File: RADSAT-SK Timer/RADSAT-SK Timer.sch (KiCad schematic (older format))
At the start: 72 parts, among them J101 Conn_02x26_Odd_Even, J103 Conn_02x26_Odd_Even, Q101 IRLML2060, Q102 IRLML2060, Q103 IRLML2060, Q104 IRLML2060, Q105 IRLML2060, Q106 IRLML2060, Q107 IRLML2060, Q108 IRLML2060, Q109 IRLML2060, U101 LM397MF, U102 LM397MF, U103 LM397MF, U104 CD4052B

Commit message: Sourced coin cell battery and tantalum caps, still need to footprint coin cell holders
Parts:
- C101, C102, C105, C106, C107, C108: footprint Capacitor_Tantalum_SMD:CP_EIA-7343-31_Kemet-D -> Capacitor_Tantalum_SMD:CP_EIA-7343-30_AVX-N_Pad2.25x2.55mm_HandSolder
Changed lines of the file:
@@
 F 0 "C101" H 2593 1721 50  0000 L CNN
 F 1 "330u" H 2593 1630 50  0000 L CNN
-F 2 "Capacitor_Tantalum_SMD:CP_EIA-7343-31_Kemet-D" H 2513 1525 50  0001 C CNN
+F 2 "Capacitor_Tantalum_SMD:CP_EIA-7343-30_AVX-N_Pad2.25x2.55mm_HandSolder" H 2513 1525 50  0001 C CNN
 F 3 "~" H 2475 1675 50  0001 C CNN
 	1    2475 1675
@@
 F 0 "C102" H 2993 1721 50  0000 L CNN
 F 1 "330u" H 2993 1630 50  0000 L CNN
-F 2 "Capacitor_Tantalum_SMD:CP_EIA-7343-31_Kemet-D" H 2913 1525 50  0001 C CNN
+F 2 "Capacitor_Tantalum_SMD:CP_EIA-7343-30_AVX-N_Pad2.25x2.55mm_HandSolder" H 2913 1525 50  0001 C CNN
 F 3 "~" H 2875 1675 50  0001 C CNN
 	1    2875 1675
@@
 F 0 "C105" H 2593 3821 50  0000 L CNN
 F 1 "330u" H 2593 3730 50  0000 L CNN
-F 2 "Capacitor_Tantalum_SMD:CP_EIA-7343-31_Kemet-D" H 2513 3625 50  0001 C CNN
+F 2 "Capacitor_Tantalum_SMD:CP_EIA-7343-30_AVX-N_Pad2.25x2.55mm_HandSolder" H 2513 3625 50  0001 C CNN
 F 3 "~" H 2475 3775 50  0001 C CNN
 	1    2475 3775
@@
 F 0 "C107" H 2993 3821 50  0000 L CNN
 F 1 "330u" H 2993 3730 50  0000 L CNN
-F 2 "Capacitor_Tantalum_SMD:CP_EIA-7343-31_Kemet-D" H 2913 3625 50  0001 C CNN
+F 2 "Capacitor_Tantalum_SMD:CP_EIA-7343-30_AVX-N_Pad2.25x2.55mm_HandSolder" H 2913 3625 50  0001 C CNN
 F 3 "~" H 2875 3775 50  0001 C CNN
 	1    2875 3775
@@
 F 0 "C106" H 2593 5871 50  0000 L CNN
 F 1 "330u" H 2593 5780 50  0000 L CNN
-F 2 "Capacitor_Tantalum_SMD:CP_EIA-7343-31_Kemet-D" H 2513 5675 50  0001 C CNN
+F 2 "Capacitor_Tantalum_SMD:CP_EIA-7343-30_AVX-N_Pad2.25x2.55mm_HandSolder" H 2513 5675 50  0001 C CNN
 F 3 "~" H 2475 5825 50  0001 C CNN
 	1    2475 5825
@@
 F 0 "C108" H 2993 5871 50  0000 L CNN
 F 1 "330u" H 2993 5780 50  0000 L CNN
-F 2 "Capacitor_Tantalum_SMD:CP_EIA-7343-31_Kemet-D" H 2913 5675 50  0001 C CNN
+F 2 "Capacitor_Tantalum_SMD:CP_EIA-7343-30_AVX-N_Pad2.25x2.55mm_HandSolder" H 2913 5675 50  0001 C CNN
 F 3 "~" H 2875 5825 50  0001 C CNN
 	1    2875 5825

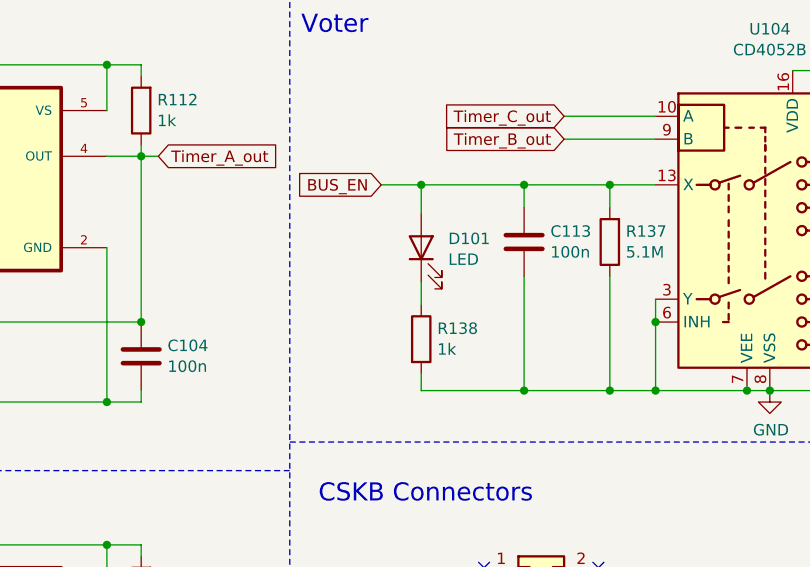
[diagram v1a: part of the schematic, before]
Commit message: the RBF relay transistor was redundant, added in another LED and updated diode configuration, resistor sourcing TBD
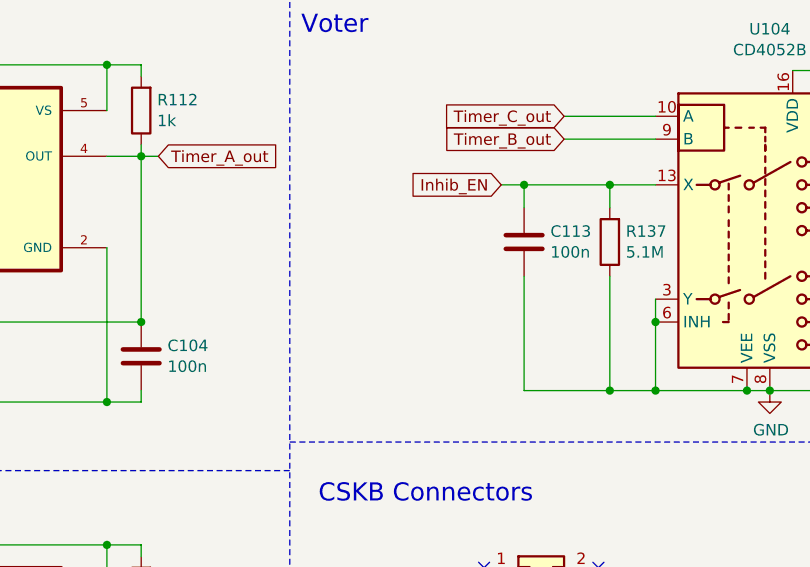
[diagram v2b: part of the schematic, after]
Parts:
- removed D101: LED, LED_SMD:LED_0603_1608Metric_Pad1.05x0.95mm_HandSolder, symbol Device:LED
- removed R138: 1k, Resistor_SMD:R_0805_2012Metric, symbol Device:R
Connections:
- net BUS_EN renamed Inhib_EN
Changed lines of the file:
@@
 Wire Wire Line
 	8225 1075 8625 1075
-Text GLabel 7425 1275 0    50   Input ~ 0
-BUS_EN
+Text GLabel 7950 1275 0    50   Input ~ 0
+Inhib_EN
 Wire Wire Line
 	9750 1325 9750 1275
@@
 	8050 2175 8425 2175
 Connection ~ 8425 2175
-Connection ~ 8050 1275
 Wire Wire Line
 	10775 775  10775 1400
@@
 NoConn ~ 10350 4225
 NoConn ~ 10350 4125
-$Comp
-L Device:LED D101
-U 1 1 600FEA55
-P 7600 1550
-F 0 "D101" V 7639 1432 50  0000 R CNN
-F 1 "LED" V 7548 1432 50  0000 R CNN
-F 2 "LED_SMD:LED_0603_1608Metric_Pad1.05x0.95mm_HandSolder" H 7600 1550 50  0001 C CNN
-F 3 "~" H 7600 1550 50  0001 C CNN
-	1    7600 1550
-	0    -1   -1   0
-$EndComp
-$Comp
-L Device:R R138
-U 1 1 60100324
-P 7600 1950
-F 0 "R138" H 7670 1996 50  0000 L CNN
-F 1 "1k" H 7670 1905 50  0000 L CNN
-F 2 "Resistor_SMD:R_0805_2012Metric" V 7530 1950 50  0001 C CNN
-F 3 "~" H 7600 1950 50  0001 C CNN
-	1    7600 1950
-	1    0    0    -1
-$EndComp
-Wire Wire Line
-	7600 1700 7600 1800
-Wire Wire Line
-	7600 1400 7600 1275
-Wire Wire Line
-	7600 1275 8050 1275
-Wire Wire Line
-	7600 1275 7425 1275
-Connection ~ 7600 1275
-Wire Wire Line
-	7600 2100 7600 2175
-Wire Wire Line
-	7600 2175 8050 2175
-Connection ~ 8050 2175
 Wire Wire Line
 	2100 2850 2875 2850
@@
 Wire Wire Line
 	8375 4150 8800 4150
+Connection ~ 8050 1275
+Wire Wire Line
+	7950 1275 8050 1275
 $EndSCHEMATC

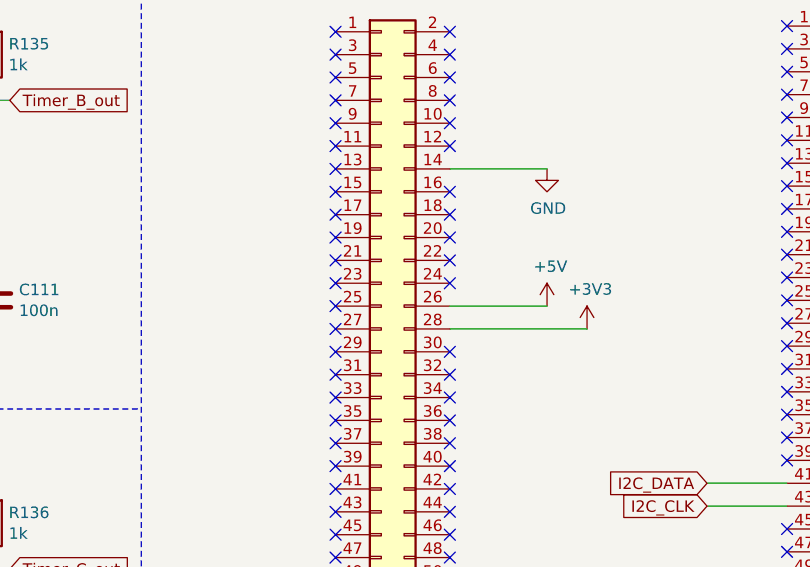
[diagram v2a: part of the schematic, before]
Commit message: Made changes to accomadate the RBF alternate charge plug
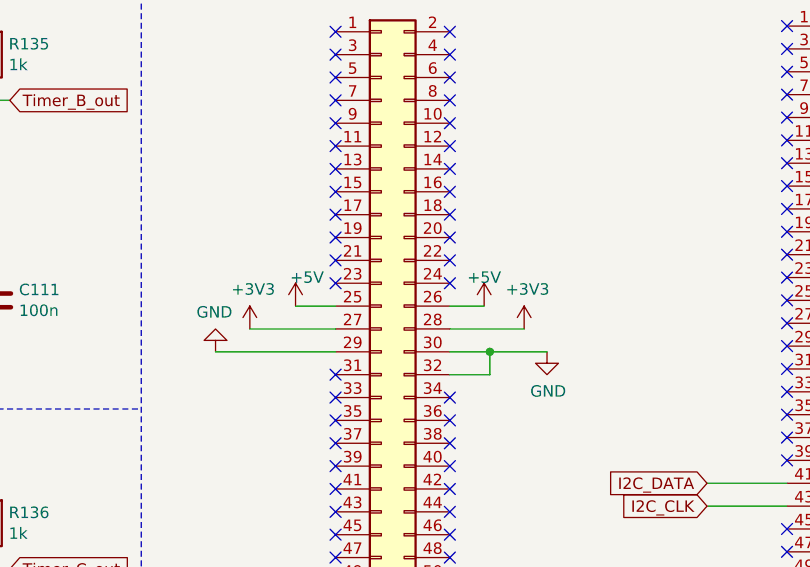
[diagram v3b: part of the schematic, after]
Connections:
- net +3V3: now also J101.27 (Pin_27)
- net +5V: now also J101.25 (Pin_25)
- net GND: now also J101.29 (Pin_29), J101.30 (Pin_30), J101.32 (Pin_32); no longer J101.14 (Pin_14)
- no-connect marks 98 -> 94
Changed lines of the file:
@@
 Text GLabel 9500 5025 0    50   Input ~ 0
 I2C_CLK
-$Comp
-L power:GND #PWR0113
-U 1 1 6038D0E1
-P 8800 3550
-F 0 "#PWR0113" H 8800 3300 50  0001 C CNN
-F 1 "GND" H 8805 3377 50  0000 C CNN
-F 2 "" H 8800 3550 50  0001 C CNN
-F 3 "" H 8800 3550 50  0001 C CNN
-	1    8800 3550
-	1    0    0    -1
-$EndComp
 Wire Notes Line
 	7025 5850 11225 5850
@@
 NoConn ~ 7875 3150
 NoConn ~ 7875 3250
-NoConn ~ 7875 3350
 NoConn ~ 7875 3450
 NoConn ~ 7875 3550
 NoConn ~ 7875 3650
-NoConn ~ 7875 3750
 NoConn ~ 7875 3850
-NoConn ~ 7875 3950
-NoConn ~ 8375 3950
 NoConn ~ 8375 4050
 NoConn ~ 7875 4050
-NoConn ~ 7875 4150
-NoConn ~ 7875 4250
-NoConn ~ 7875 4350
-NoConn ~ 8375 4350
-NoConn ~ 8375 4450
 NoConn ~ 7875 4450
 NoConn ~ 7875 4550
@@
 	1    0    0    -1
 $EndComp
-Wire Wire Line
-	8375 3550 8800 3550
 NoConn ~ 10350 3525
 NoConn ~ 10350 4225
@@
 L power:+5V #PWR0114
 U 1 1 6039ECF2
-P 8800 4150
-F 0 "#PWR0114" H 8800 4000 50  0001 C CNN
-F 1 "+5V" H 8815 4323 50  0000 C CNN
-F 2 "" H 8800 4150 50  0001 C CNN
-F 3 "" H 8800 4150 50  0001 C CNN
-	1    8800 4150
-	1    0    0    -1
-$EndComp
-Wire Wire Line
-	8375 4250 8975 4250
+P 8525 4150
+F 0 "#PWR0114" H 8525 4000 50  0001 C CNN
+F 1 "+5V" H 8525 4275 50  0000 C CNN
+F 2 "" H 8525 4150 50  0001 C CNN
+F 3 "" H 8525 4150 50  0001 C CNN
+	1    8525 4150
+	1    0    0    -1
+$EndComp
 $Comp
 L power:+3V3 #PWR0115
 U 1 1 603B0D07
-P 8975 4250
-F 0 "#PWR0115" H 8975 4100 50  0001 C CNN
-F 1 "+3V3" H 8990 4423 50  0000 C CNN
-F 2 "" H 8975 4250 50  0001 C CNN
-F 3 "" H 8975 4250 50  0001 C CNN
-	1    8975 4250
-	1    0    0    -1
-$EndComp
-Wire Wire Line
-	8375 4150 8800 4150
+P 8700 4250
+F 0 "#PWR0115" H 8700 4100 50  0001 C CNN
+F 1 "+3V3" H 8715 4423 50  0000 C CNN
+F 2 "" H 8700 4250 50  0001 C CNN
+F 3 "" H 8700 4250 50  0001 C CNN
+	1    8700 4250
+	1    0    0    -1
+$EndComp
 Connection ~ 8050 1275
 Wire Wire Line
 	7950 1275 8050 1275
+$Comp
+L power:+5V #PWR?
+U 1 1 61821443
+P 7700 4150
+F 0 "#PWR?" H 7700 4000 50  0001 C CNN
+F 1 "+5V" H 7750 4275 50  0000 C CNN
+F 2 "" H 7700 4150 50  0001 C CNN
+F 3 "" H 7700 4150 50  0001 C CNN
+	1    7700 4150
+	1    0    0    -1
+$EndComp
+$Comp
+L power:+3V3 #PWR?
+U 1 1 61821449
+P 7500 4250
+F 0 "#PWR?" H 7500 4100 50  0001 C CNN
+F 1 "+3V3" H 7515 4423 50  0000 C CNN
+F 2 "" H 7500 4250 50  0001 C CNN
+F 3 "" H 7500 4250 50  0001 C CNN
+	1    7500 4250
+	1    0    0    -1
+$EndComp
+Wire Wire Line
+	7700 4150 7875 4150
+Wire Wire Line
+	7875 4250 7500 4250
+Wire Wire Line
+	8375 4150 8525 4150
+Wire Wire Line
+	8375 4250 8700 4250
+$Comp
+L power:GND #PWR?
+U 1 1 618A8198
+P 8800 4350
+F 0 "#PWR?" H 8800 4100 50  0001 C CNN
+F 1 "GND" H 8805 4177 50  0000 C CNN
+F 2 "" H 8800 4350 50  0001 C CNN
+F 3 "" H 8800 4350 50  0001 C CNN
+	1    8800 4350
+	1    0    0    -1
+$EndComp
+Wire Wire Line
+	8375 4350 8550 4350
+$Comp
+L power:GND #PWR?
+U 1 1 618C6C97
+P 7350 4350
+F 0 "#PWR?" H 7350 4100 50  0001 C CNN
+F 1 "GND" H 7355 4177 50  0000 C CNN
+F 2 "" H 7350 4350 50  0001 C CNN
+F 3 "" H 7350 4350 50  0001 C CNN
+	1    7350 4350
+	-1   0    0    1
+$EndComp
+Wire Wire Line
+	7350 4350 7875 4350
+NoConn ~ 8375 3550
+NoConn ~ 7875 3350
+NoConn ~ 7875 3750
+NoConn ~ 7875 3950
+NoConn ~ 8375 3950
+Wire Wire Line
+	8375 4450 8550 4450
+Wire Wire Line
+	8550 4450 8550 4350
+Connection ~ 8550 4350
+Wire Wire Line
+	8550 4350 8800 4350
 $EndSCHEMATC
